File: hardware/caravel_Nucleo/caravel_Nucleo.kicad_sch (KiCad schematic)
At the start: 106 parts, among them IC1 74LVC2G32DP,125, J1 USB4105-GF-A, J10 PinHeader_1x11, J11 PinHeader_1x02, J12 PinHeader_1x02, J13 PinHeader_1x02, J2 PinHeader_1x02, J3 PinHeader_1x02, J4 61300411121, J5 PinHeader_1x02, J6 PinHeader_1x02, J7 61300611121, J8 640456-3, J9 640456-3, Q1 BSS84AKW, SW1 KMR2, T1 Logo, T2 Logo, U1 FT232HQ, U12 NUCLEO144-F429ZI, U2 SN74LVC1G125DCKR, U3 SN74LVC1G125DCKR, U4 MAX811REUS+T, U5 MCP4661-103E/ML, U6 Caravel_breakout_PCB, U7 W25Q32FVSS, U8 NTS0102DP, U9 MIC2211-AAYML-TR, X1 ECS-2520MVLC-100-BN-TR, Y1 ABM8G-12.000MHZ-18-D2Y-T

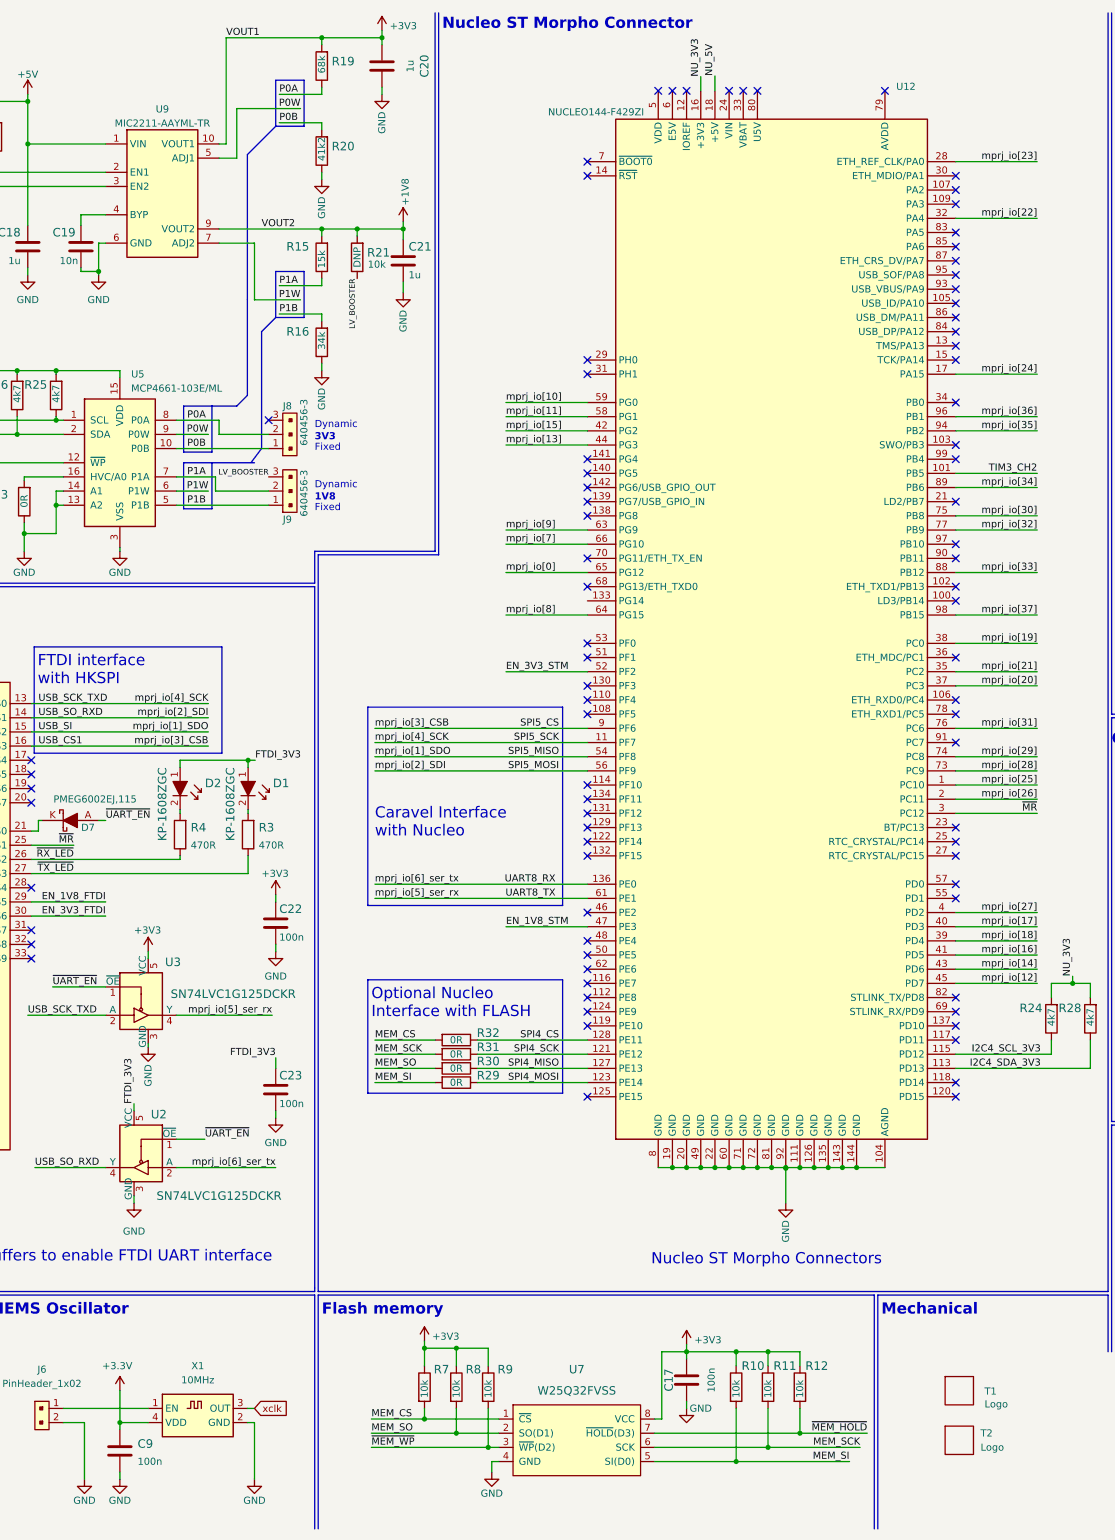
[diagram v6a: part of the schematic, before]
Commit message: Update components in schematic. Annotation
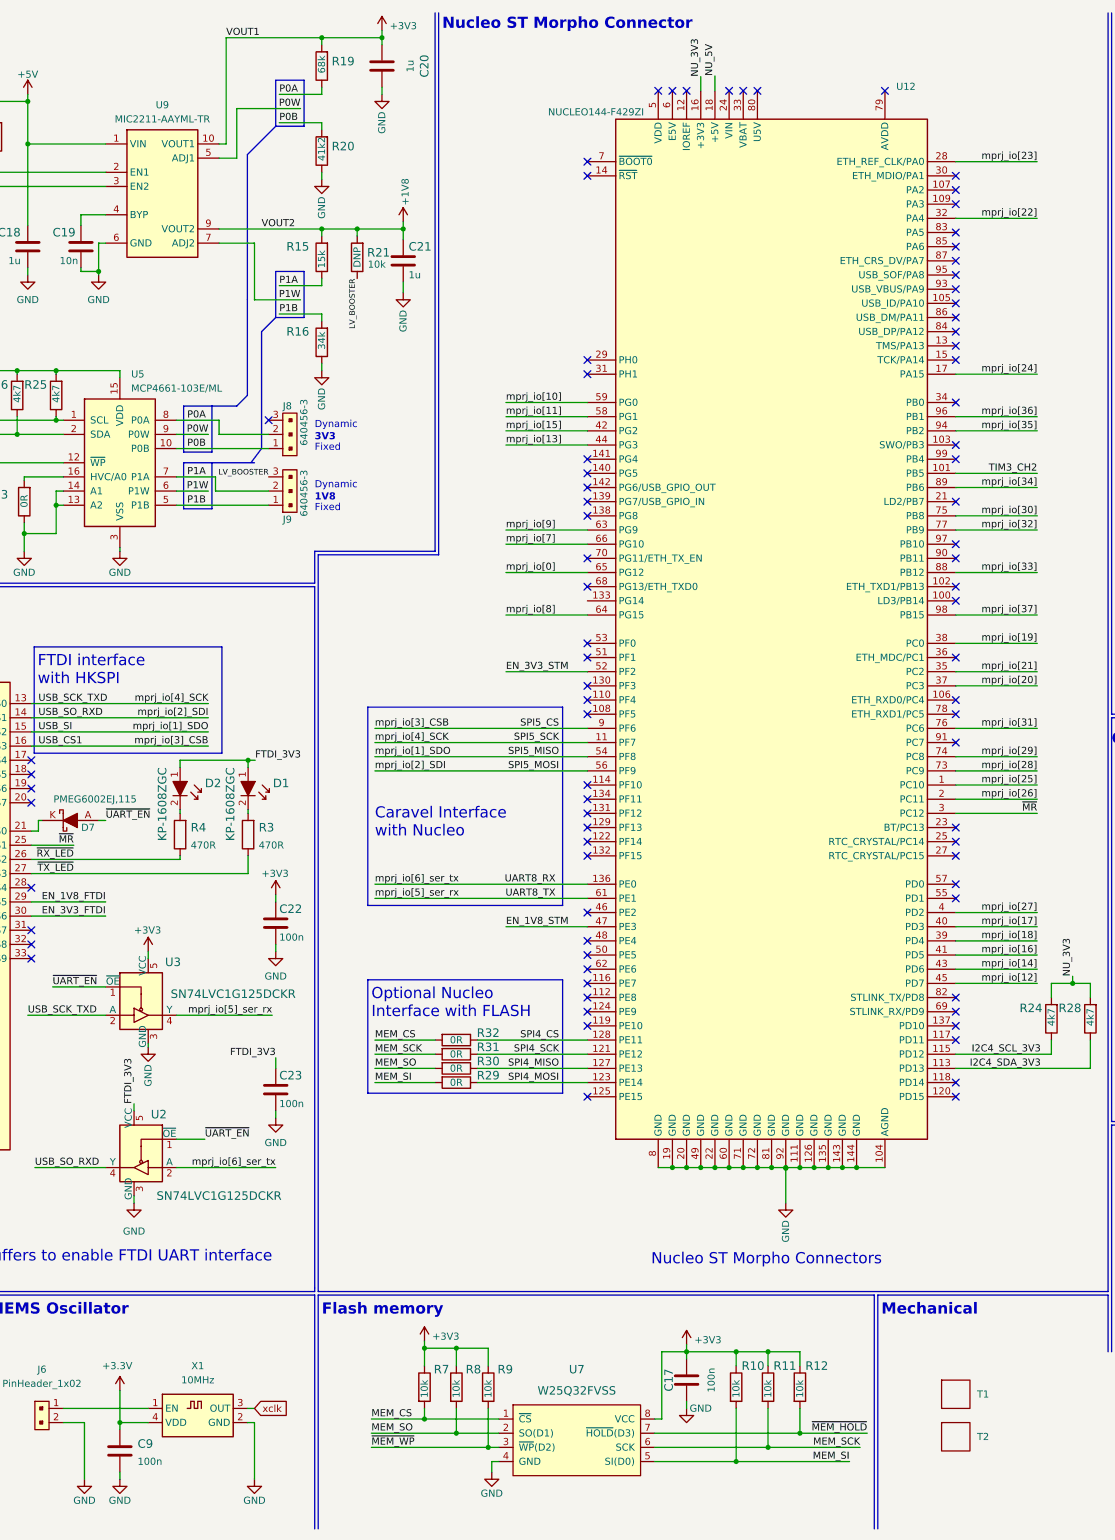
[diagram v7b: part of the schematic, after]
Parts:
- removed T1: Logo, antmicro-footprints:efabless_logo_2, symbol Caravel_board:Logo
- removed T2: Logo, antmicro-footprints:efabless_logo, symbol Caravel_board:Logo
- removed U9: MIC2211-AAYML-TR, antmicro-footprints:DFN-10-1EP_3x3mm, symbol antmicroPMICVoltageRegulatorsLinear:MIC2211-AAYML-TR
- added T1, T2: efabless_logo, caravel_Nucleo-footprints:efabless_logo, symbol caravel_Nucleo:efabless_logo
- added U9: MIC2211-AAYML-TR, caravel_Nucleo-footprints:DFN-10-1EP_3x3mm, symbol caravel_Nucleo:MIC2211-AAYML-TR
- C1, C19: footprint antmicro-footprints:0603-cap -> caravel_Nucleo-footprints:0603-cap; symbol antmicroCapacitors0603:C_10n_0603 -> caravel_Nucleo:C_10n_0603
- C10, C14: footprint antmicro-footprints:0603-cap -> caravel_Nucleo-footprints:0603-cap; symbol antmicroCapacitors0603:C_4u7_0603 -> caravel_Nucleo:C_4u7_0603
- C11, C13: footprint antmicro-footprints:0603-cap -> caravel_Nucleo-footprints:0603-cap; symbol antmicroCapacitors0603:C_18p_0603 -> caravel_Nucleo:C_18p_0603
- C12, C15, C16, C17, C2, C22, C23, C24, C25, C26, C27, C28, C29, C3, C30, C31, C32, C33, C34, C35, C36, C4, C5, C6, C7, C8, C9: footprint antmicro-footprints:0603-cap -> caravel_Nucleo-footprints:0603-cap; symbol antmicroCapacitors0603:C_100n_0603 -> caravel_Nucleo:C_100n_0603
- C18, C20, C21: footprint antmicro-footprints:0603-cap -> caravel_Nucleo-footprints:0603-cap; symbol antmicroCapacitors0603:C_1u_0603 -> caravel_Nucleo:C_1u_0603
- D1, D2, D3, D4: footprint antmicro-footprints:LED_0603 -> caravel_Nucleo-footprints:LED_0603; symbol antmicroLEDIndicationDiscrete:KP-1608ZGC -> caravel_Nucleo:KP-1608ZGC
- D5, D6: footprint antmicro-footprints:SOD-123 -> caravel_Nucleo-footprints:SOD-123; symbol antmicroDiodesRectifiersSingle:1N5819HW-7-F -> caravel_Nucleo:1N5819HW-7-F
- D7: footprint antmicro-footprints:SOD-323F -> caravel_Nucleo-footprints:SOD-323F; symbol antmicroDiodesRectifiersSingle:PMEG6002EJ,115 -> caravel_Nucleo:PMEG6002EJ,115
- IC1: footprint antmicro-footprints:TSSOP-8_W3mm -> caravel_Nucleo-footprints:TSSOP-8_W3mm; symbol antmicroLogicGatesandInverters:74LVC2G32DP,125 -> caravel_Nucleo:74LVC2G32DP,125
- J1: footprint antmicro-footprints:GCT_USB4105-GF-A -> caravel_Nucleo-footprints:GCT_USB4105-GF-A; symbol antmicroUSBDVIHDMIConnectors:USB4105-GF-A -> caravel_Nucleo:USB4105-GF-A
- J10: footprint antmicro-footprints:PinHeader_1x11_P2.54_Vertical -> caravel_Nucleo-footprints:PinHeader_1x11_P2.54_Vertical; symbol antmicroRectangularConnectorsHeadersMalePins:PinHeader_1x11 -> caravel_Nucleo:PinHeader_1x11
- J11, J12, J13, J2, J3, J5, J6: footprint antmicro-footprints:PinHeader_1x2_P2.54mm -> caravel_Nucleo-footprints:PinHeader_1x2_P2.54mm; symbol antmicroRectangularConnectorsHeadersMalePins:PinHeader_1x02 -> caravel_Nucleo:PinHeader_1x02
- J4: footprint antmicro-footprints:PinHeader_1x4_P2.54mm_Drill1.02mm -> caravel_Nucleo-footprints:PinHeader_1x4_P2.54mm_Drill1.02mm; symbol antmicroRectangularConnectorsHeadersMalePins:61300411121 -> caravel_Nucleo:61300411121
- J7: footprint antmicro-footprints:61300611121 -> caravel_Nucleo-footprints:61300611121; symbol antmicroRectangularConnectorsHeadersMalePins:61300611121 -> caravel_Nucleo:61300611121
- J8, J9: footprint antmicro-footprints:PinHeader_1x3_P2.54_Drill1.1mm -> caravel_Nucleo-footprints:PinHeader_1x3_P2.54_Drill1.1mm; symbol antmicroRectangularConnectorsHeadersMalePins:640456-3 -> caravel_Nucleo:640456-3
- Q1: footprint antmicro-footprints:SOT-323 -> caravel_Nucleo-footprints:SOT-323; symbol antmicroTransistorsFETsMOSFETsSingle:BSS84AKW -> caravel_Nucleo:BSS84AKW
- R1, R10, R11, R12, R17, R18, R21, R22, R23, R27, R7, R8, R9: footprint antmicro-footprints:0603-res -> caravel_Nucleo-footprints:0603-res; symbol antmicroResistors0603:R_10k_0603 -> caravel_Nucleo:R_10k_0603
- R13, R14, R3, R4: footprint antmicro-footprints:0603-res -> caravel_Nucleo-footprints:0603-res; symbol antmicroResistors0603:R_470R_0603 -> caravel_Nucleo:R_470R_0603
- R15: footprint antmicro-footprints:0603-res -> caravel_Nucleo-footprints:0603-res; symbol antmicroResistors0603:R_15k_0603 -> caravel_Nucleo:R_15k_0603
- R16: footprint antmicro-footprints:0603-res -> caravel_Nucleo-footprints:0603-res; symbol antmicroResistors0603:R_34k_0603 -> caravel_Nucleo:R_34k_0603
- R19: footprint antmicro-footprints:0603-res -> caravel_Nucleo-footprints:0603-res; symbol antmicroResistors0603:R_68k_0603 -> caravel_Nucleo:R_68k_0603
- R2: footprint antmicro-footprints:0603-res -> caravel_Nucleo-footprints:0603-res; symbol antmicroResistors0603:R_12k_0603 -> caravel_Nucleo:R_12k_0603
- R20: footprint antmicro-footprints:0603-res -> caravel_Nucleo-footprints:0603-res; symbol antmicroResistors0603:R_41k2_0603 -> caravel_Nucleo:R_41k2_0603
- R24, R25, R26, R28: footprint antmicro-footprints:0603-res -> caravel_Nucleo-footprints:0603-res; symbol antmicroResistors0603:R_4k7_0603 -> caravel_Nucleo:R_4k7_0603
- R29, R30, R31, R32, R33: footprint antmicro-footprints:0603-res -> caravel_Nucleo-footprints:0603-res; symbol antmicroResistors0603:R_0R_0603 -> caravel_Nucleo:R_0R_0603
- R5, R6: footprint antmicro-footprints:0603-res -> caravel_Nucleo-footprints:0603-res; symbol antmicroResistors0603:R_5k1_0603 -> caravel_Nucleo:R_5k1_0603
- SW1: footprint antmicro-footprints:SW_SPST_4.2x2.8 -> caravel_Nucleo-footprints:SW_SPST_4.2x2.8; symbol antmicroPushbuttonSwitches:KMR2 -> caravel_Nucleo:KMR2
- U1: footprint antmicro-footprints:QFN-48-1EP_8x8mm_P0.5mm_EP6.2x6.2mm_FT232HQ_marking -> caravel_Nucleo-footprints:QFN-48-1EP_8x8mm_P0.5mm_EP6.2x6.2mm_FT232HQ_marking; symbol antmicroInterfaceControllers:FT232HQ -> caravel_Nucleo:FT232HQ
- U12: footprint antmicro-footprints:ST_Morpho_Connectors_144 -> caravel_Nucleo-footprints:ST_Morpho_Connectors_144; symbol antmicroModules:NUCLEO144-F429ZI -> caravel_Nucleo:NUCLEO144-F429ZI
- U2, U3: footprint antmicro-footprints:SOT-353 -> caravel_Nucleo-footprints:SOT-353; symbol antmicroLogicBuffersDriversReceiversTransceivers:SN74LVC1G125DCKR -> caravel_Nucleo:SN74LVC1G125DCKR
- U4: footprint antmicro-footprints:SOT-143-4 -> caravel_Nucleo-footprints:SOT-143-4; symbol antmicroPMICPowerSequencers:MAX811REUS+T -> caravel_Nucleo:MAX811REUS+T
- U5: footprint antmicro-footprints:QFN-16_EP_4x4_Pitch0.65mm -> caravel_Nucleo-footprints:QFN-16_EP_4x4_Pitch0.65mm; symbol antmicroInterfaceIOExpanders:MCP4661-103E/ML -> caravel_Nucleo:MCP4661-103E/ML
- U6: footprint antmicro-footprints:caravel_breakout -> caravel_Nucleo-footprints:caravel_breakout; symbol antmicroModules:Caravel_breakout_PCB -> caravel_Nucleo:Caravel_breakout_PCB
- U7: footprint antmicro-footprints:SOIC127P790X216-8N -> caravel_Nucleo-footprints:SOIC127P790X216-8N; symbol antmicroMemory:W25Q32FVSS -> caravel_Nucleo:W25Q32FVSS
- U8: footprint antmicro-footprints:TSSOP-8_W3mm -> caravel_Nucleo-footprints:TSSOP-8_W3mm; symbol antmicroLogicTranslatorsLevelShifters:NTS0102DP -> caravel_Nucleo:NTS0102DP
- X1: footprint antmicro-footprints:Oscillator_SMD_ECS_2520MV-xxx-xx-4Pin_2.5x2.0mm -> caravel_Nucleo-footprints:Oscillator_SMD_ECS_2520MV-xxx-xx-4Pin_2.5x2.0mm; symbol antmicroCrystals:ECS-2520MVLC-100-BN-TR -> caravel_Nucleo:ECS-2520MVLC-100-BN-TR
- Y1: footprint antmicro-footprints:KX-7 -> caravel_Nucleo-footprints:KX-7; symbol antmicroCrystals:ABM8G-12.000MHZ-18-D2Y-T -> caravel_Nucleo:ABM8G-12.000MHZ-18-D2Y-T
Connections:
- net +1V8: now also U9.9 (VOUT2)
- net +3V3: now also U9.10 (VOUT1)
- net +5V: now also U9.1 (VIN)
- net AGND: now also U9.11 (EP), U9.6 (GND)
- net EN_VOUT1: now also U9.2 (EN1)
- net EN_VOUT2: now also U9.3 (EN2)
- net P0W: now also U9.5 (ADJ1)
- net P1W: now also U9.7 (ADJ2)
- net at C19.2: now also U9.4 (BYP)

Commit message: Update Efabless logo on schematics
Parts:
- T1: footprint caravel_Nucleo-footprints:efabless_logo -> caravel_Nucleo-footprints:logo
